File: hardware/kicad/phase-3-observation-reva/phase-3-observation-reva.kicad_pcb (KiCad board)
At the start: 2 copper layers, 95 x 65 mm, 20 parts, among them J1 MONITOR_INPUT, J2 HOST_IF, J3 SPARE_IF, U1 TLV9064IDR, U2 ADS1114IDGS, U3 74LVC1G17GW, U4 74LVC1G17GW

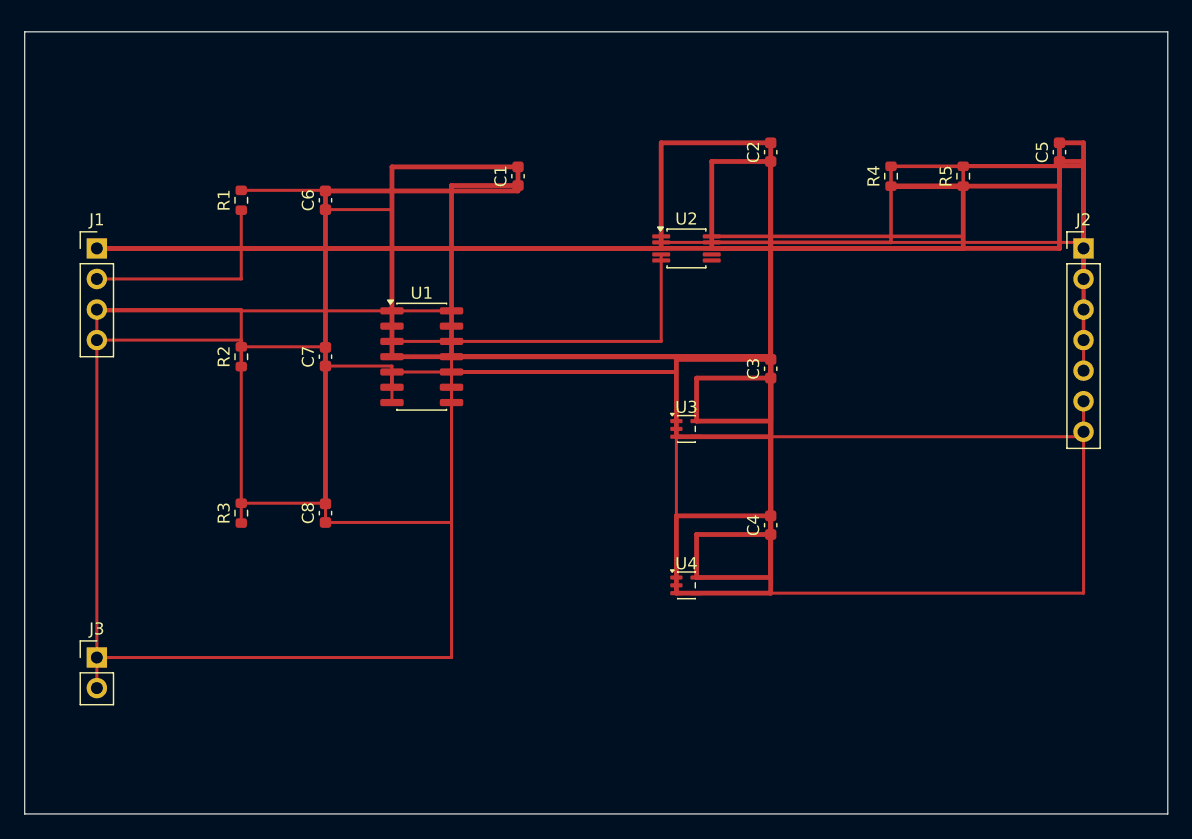
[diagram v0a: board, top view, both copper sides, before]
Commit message: Complete phase 3 observation circuit fabrication files
- Lock final part selection: ADS1115IDGSR (sub for ADS1114), TLV9064IDR,
  74LVC1G17GW x2; all passives on 0402 with verified LCSC part numbers
- Update schematic symbol fields (MPNs, footprints) and link 3D models
- Add custom symbol library (ADS1115IDGSR MSOP-10)
- Generate production files via Fabrication Toolkit: Gerbers, BOM with
  LCSC numbers, CPL with corrected IC rotations (U1/U2 270°, U3/U4 180°)
- Update phase-3-execution.md with final BOM table, LCSC numbers,
  fabrication file inventory, and revised status
- Extend .gitignore with production/ subdirectory noise patterns

Co-Authored-By: Claude Sonnet 4.6 <noreply@anthropic.com>
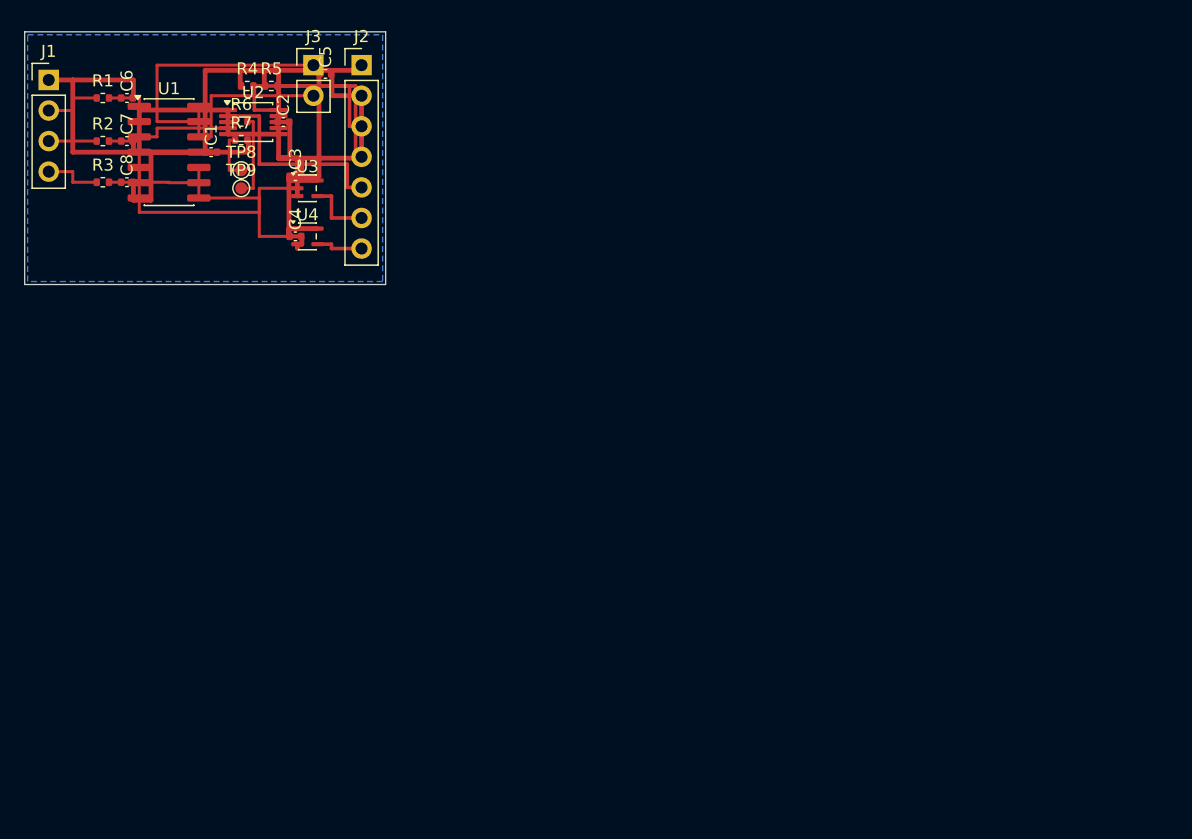
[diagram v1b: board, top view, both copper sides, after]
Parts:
- added R6: 0, Resistor_SMD:R_0402_1005Metric, F.Cu at (18.0, 7.46)
- added R7: 0, Resistor_SMD:R_0402_1005Metric, F.Cu at (18.0, 9.00)
- added TP8: U1D_IN, TestPoint:TestPoint_Pad_D1.0mm, F.Cu at (18.0, 11.5)
- added TP9: U1D_OUT, TestPoint:TestPoint_Pad_D1.0mm, F.Cu at (18.0, 13.0)
- C1, C2, C3, C4, C5, C6, C7, C8: footprint C_0603_1608Metric -> Capacitor_SMD:C_0402_1005Metric
- J1: footprint PinHeader_1x04_P2.54mm_Vertical -> Connector_PinHeader_2.54mm:PinHeader_1x04_P2.54mm_Vertical
- J2: footprint PinHeader_1x07_P2.54mm_Vertical -> Connector_PinHeader_2.54mm:PinHeader_1x07_P2.54mm_Vertical
- J3: footprint PinHeader_1x02_P2.54mm_Vertical -> Connector_PinHeader_2.54mm:PinHeader_1x02_P2.54mm_Vertical
- R1, R2, R3, R4, R5: footprint R_0603_1608Metric -> Resistor_SMD:R_0402_1005Metric
- U1: footprint SOIC-14_3.9x8.7mm_P1.27mm -> Package_SO:SOIC-14_3.9x8.7mm_P1.27mm
- U2: value ADS1114IDGS -> ADS1115IDGSR; footprint MSOP-10_3x3mm_P0.5mm -> Package_SO:MSOP-10_3x3mm_P0.5mm
- U3, U4: footprint SOT-353_SC-70-5 -> Package_TO_SOT_SMD:SOT-353_SC-70-5
- moved J2 61.9 mm to (28.0, 2.77)
- moved C5 61.3 mm to (25.0, 3.50), turned to 0 degrees
- moved R5 58.0 mm to (20.5, 4.50), turned to 0 degrees
- moved R4 54.0 mm to (18.5, 4.50), turned to 0 degrees
- moved J3 52.4 mm to (24.0, 2.77)
- moved C4 46.2 mm to (22.5, 17.0), turned to 0 degrees
- moved U4 42.8 mm to (23.5, 17.0)
- moved C3 42.6 mm to (22.5, 12.0), turned to 0 degrees
- moved C2 40.6 mm to (21.5, 7.50), turned to 0 degrees
- moved U2 37.5 mm to (19.0, 7.50)
- moved U3 37.3 mm to (23.5, 13.0)
- moved C8 32.1 mm to (8.50, 12.5), turned to 0 degrees
- moved R3 29.8 mm to (6.50, 12.5), turned to 0 degrees
- moved U1 27.0 mm to (12.0, 10.0)
- moved C1 25.6 mm to (15.5, 10.0), turned to 0 degrees
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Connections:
- U2 pad 6: (no net) -> /GND
- U2 pad 7: (no net) -> /GND
- U3 pad 1: (no net) -> unconnected-(U3-NC-Pad1)
- U4 pad 1: (no net) -> unconnected-(U4-NC-Pad1)
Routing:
- net /GND: track 369.9 -> 95.0 mm
- net /+3V3: track 200.5 -> 53.5 mm
- net /SPARE_BUF: track 63.4 -> 15.5 mm
- net /LED_IN_GPIO: track 45.6 -> 4.02 mm
- net /I2C_SCL: track 51.2 -> 14.8 mm
- net /SPARE_IN_RAW: track 57.0 -> 21.2 mm
- net /I2C_SDA: track 49.1 -> 16.8 mm
- net /KEY1_IN_GPIO: track 35.1 -> 5.48 mm
- net /ADC_ALERT: track 45.8 -> 17.0 mm
- net /KEY_LED_BUF: track 39.0 -> 13.9 mm
- net /KEY_LED_SENSE: track 30.3 -> 7.43 mm
- net /KEY_LED_RAW: track 27.2 -> 4.79 mm
- net /KEY_ADC2_BUF: track 32.1 -> 10.6 mm
- net /KEY_ADC2_SENSE: track 23.8 -> 4.40 mm
- net /KEY_ADC1_RAW: track 16.7 -> 3.91 mm
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- added copper zone on B.Cu, net /GND
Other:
- board size 95 x 65 mm -> 30 x 21 mm
- rule pad_to_mask_clearance: 0 -> 0.05

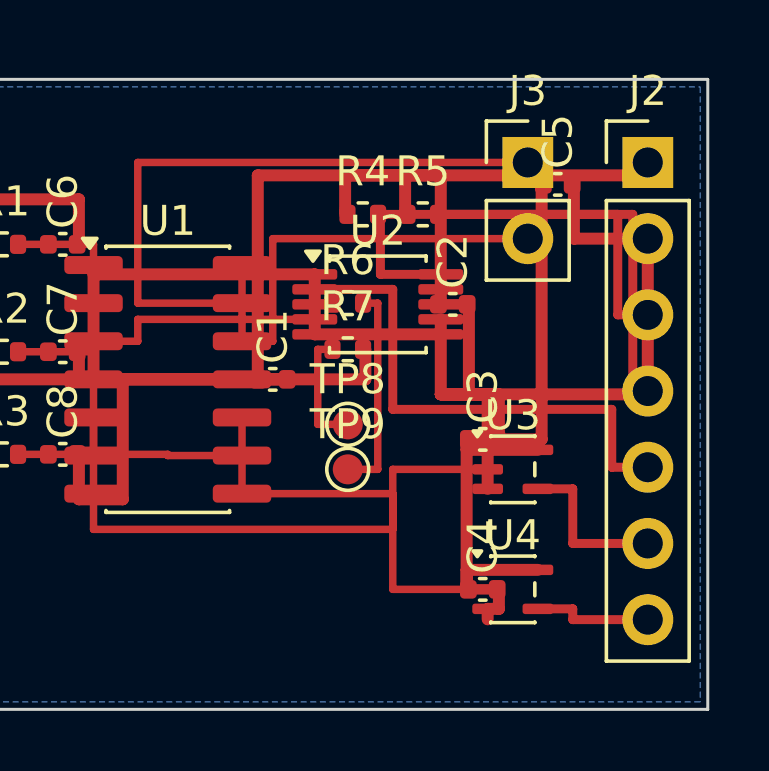
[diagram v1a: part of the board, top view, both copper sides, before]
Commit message: Fix PCB overlaps, remove DNP from C6-C8, regenerate BOM and CPL
- Move R6 (18,7.46)→(21.5,11) and R7 (18,9)→(23.5,11): both were inside
  U2 MSOP-10 courtyard, now clear with 1.2mm+ spacing
- Move C3 (22.5,12)→(20.5,13) and C4 (22.5,17)→(20.5,17): were overlapping
  U3/U4 SOT-353 courtyards, now 0.87mm clear
- Move C5 (25,3.5)→(25,8): was overlapping J3 courtyard, now clear
- Remove DNP flag and "DNP" suffix from C6/C7/C8 value: these filter caps
  were changed from DNP to populated in the schematic corrections
- production/bom.csv: add C6/C7/C8 row (LCSC C1588, 1nF C0G 0402)
- production/positions.csv: regenerate with all updated positions, add
  C6/C7/C8 (previously absent due to DNP), all rotations reflect current PCB

Note: J3, R6, R7, TP8, TP9 exist in PCB but have no schematic symbols.
These were added directly to the PCB layout and need to be reconciled in
KiCad schematic editor in a follow-up pass.

Co-Authored-By: Claude Sonnet 4.6 <noreply@anthropic.com>
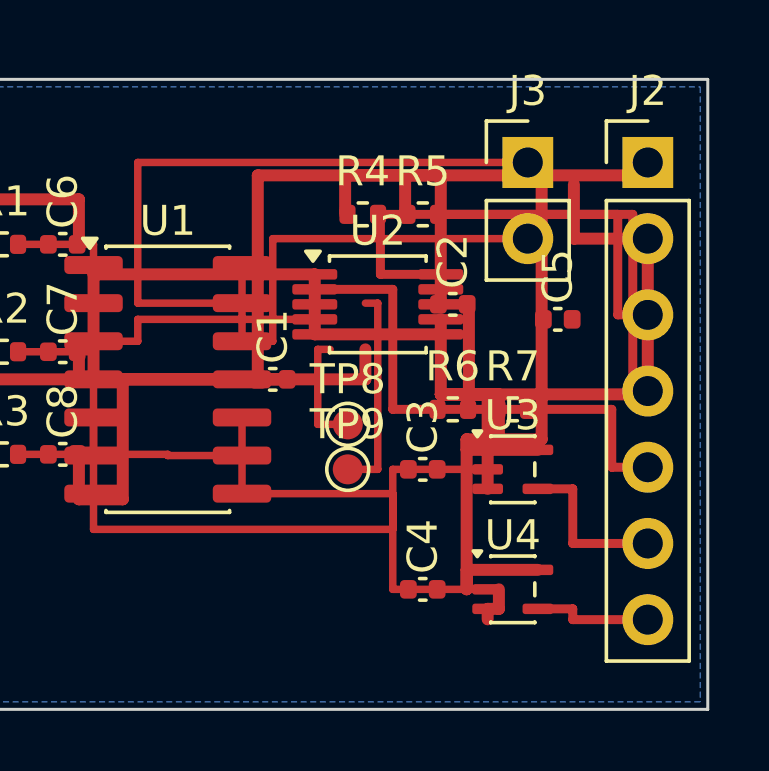
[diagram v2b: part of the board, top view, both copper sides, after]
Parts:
- C6, C7, C8: value 1n DNP -> 1n
- moved R7 5.85 mm to (23.5, 11.0)
- moved R6 4.98 mm to (21.5, 11.0)
- moved C5 4.50 mm to (25.0, 8.00)
- moved C3 2.24 mm to (20.5, 13.0)
- moved C4 2.00 mm to (20.5, 17.0)
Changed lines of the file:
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@@
 	(footprint "Resistor_SMD:R_0402_1005Metric"
 		(layer "F.Cu")
-		(at 18 7.46)
+		(at 21.5 11)
 		(descr "Resistor SMD 0402 (1005 Metric), square (rectangular) end terminal, IPC-7351 nominal, (Body size source: IPC-SM-782 page 72, https://www.pcb-3d.com/wordpress/wp-content/uploads/ipc-sm-782a_amendment_1_and_2.pdf)")
 		(tags "resistor")
@@
 	(footprint "Resistor_SMD:R_0402_1005Metric"
 		(layer "F.Cu")
-		(at 18 9)
+		(at 23.5 11)
 		(descr "Resistor SMD 0402 (1005 Metric), square (rectangular) end terminal, IPC-7351 nominal, (Body size source: IPC-SM-782 page 72, https://www.pcb-3d.com/wordpress/wp-content/uploads/ipc-sm-782a_amendment_1_and_2.pdf)")
 		(tags "resistor")
@@
 	(footprint "Capacitor_SMD:C_0402_1005Metric"
 		(layer "F.Cu")
-		(at 22.5 12)
+		(at 20.5 13)
 		(descr "Capacitor SMD 0402 (1005 Metric), square (rectangular) end terminal, IPC-7351 nominal, (Body size source: IPC-SM-782 page 76, https://www.pcb-3d.com/wordpress/wp-content/uploads/ipc-sm-782a_amendment_1_and_2.pdf)")
 		(tags "capacitor")
@@
 	(footprint "Capacitor_SMD:C_0402_1005Metric"
 		(layer "F.Cu")
-		(at 22.5 17)
+		(at 20.5 17)
 		(descr "Capacitor SMD 0402 (1005 Metric), square (rectangular) end terminal, IPC-7351 nominal, (Body size source: IPC-SM-782 page 76, https://www.pcb-3d.com/wordpress/wp-content/uploads/ipc-sm-782a_amendment_1_and_2.pdf)")
 		(tags "capacitor")
@@
 	(footprint "Capacitor_SMD:C_0402_1005Metric"
 		(layer "F.Cu")
-		(at 25 3.5)
+		(at 25 8)
 		(descr "Capacitor SMD 0402 (1005 Metric), square (rectangular) end terminal, IPC-7351 nominal, (Body size source: IPC-SM-782 page 76, https://www.pcb-3d.com/wordpress/wp-content/uploads/ipc-sm-782a_amendment_1_and_2.pdf)")
 		(tags "capacitor")
@@
 			)
 		)
-		(property "Value" "1n DNP"
+		(property "Value" "1n"
 			(at 0 1.43 90)
 			(layer "F.Fab")
@@
 			)
 		)
-		(attr smd dnp)
+		(attr smd)
 		(duplicate_pad_numbers_are_jumpers no)
 		(fp_line
@@
 			)
 		)
-		(property "Value" "1n DNP"
+		(property "Value" "1n"
 			(at 0 1.43 90)
 			(layer "F.Fab")
@@
 			)
 		)
-		(attr smd dnp)
+		(attr smd)
 		(duplicate_pad_numbers_are_jumpers no)
 		(fp_line
@@
 			)
 		)
-		(property "Value" "1n DNP"
+		(property "Value" "1n"
 			(at 0 1.43 90)
 			(layer "F.Fab")
@@
 			)
 		)
-		(attr smd dnp)
+		(attr smd)
 		(duplicate_pad_numbers_are_jumpers no)
 		(fp_line
